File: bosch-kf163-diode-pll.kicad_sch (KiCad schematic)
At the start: 49 parts, among them U1 PLL

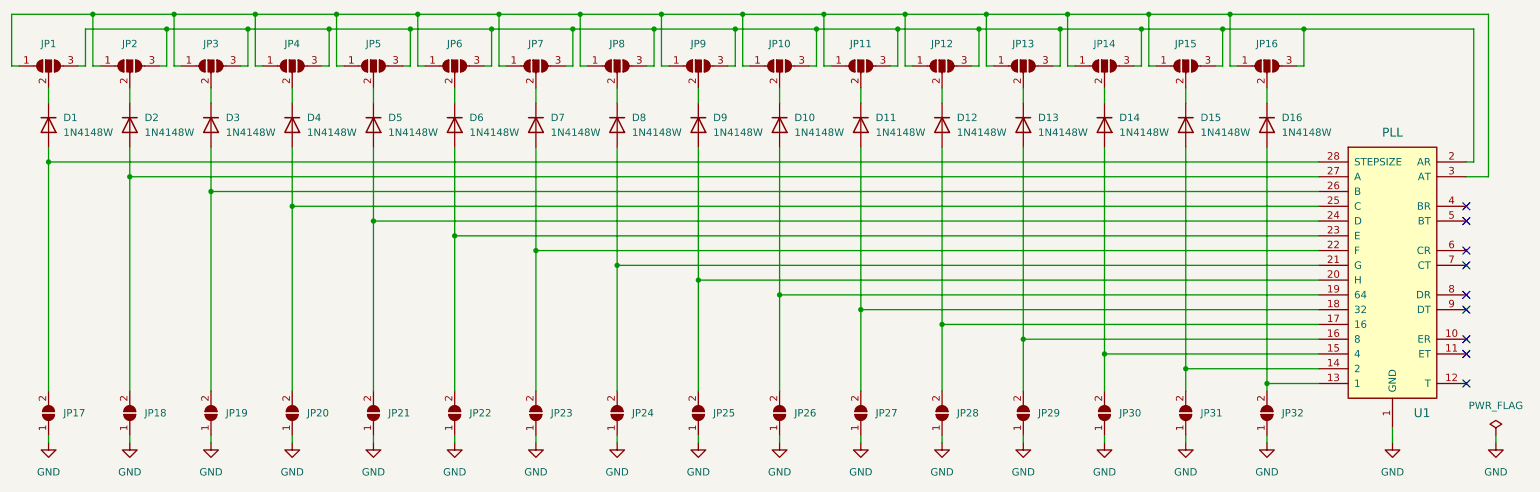
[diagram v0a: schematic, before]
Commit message: changed to smaller diodes, added schematic pdf and gerbers
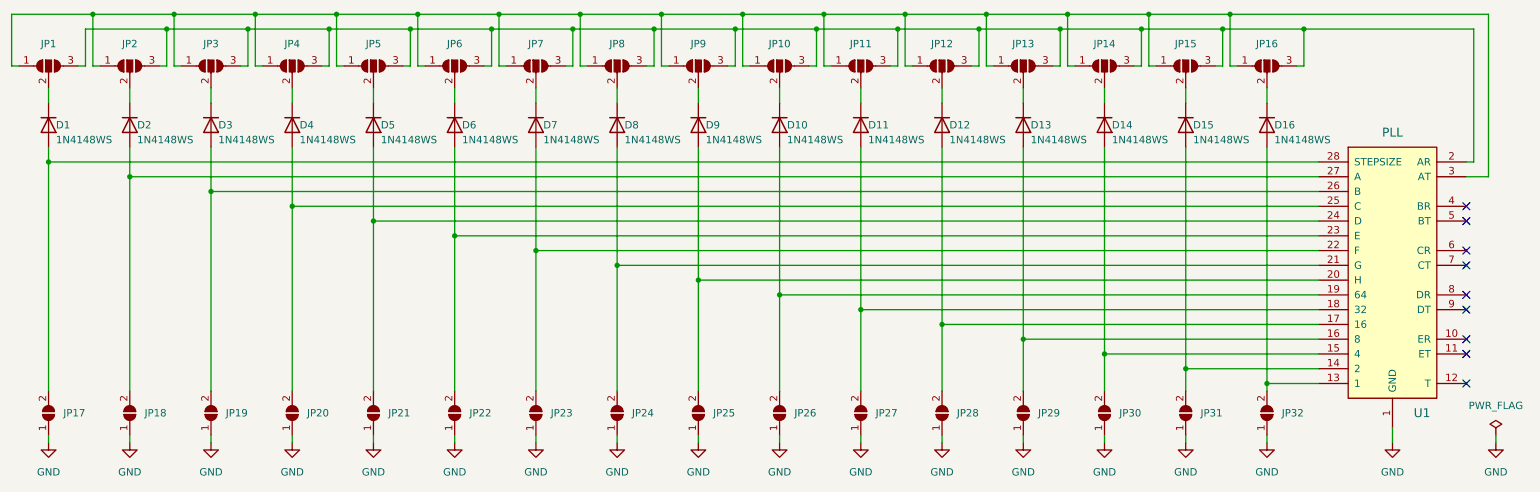
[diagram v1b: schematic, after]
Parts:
- D1, D10, D11, D12, D13, D14, D15, D16, D2, D3, D4, D5, D6, D7, D8, D9: value 1N4148W -> 1N4148WS; footprint Diode_SMD:D_SOD-123 -> Diode_SMD:D_SOD-323; LCSC C84367 -> C108805
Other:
- title: Bosch KFx3/KFx5 Diode PLL -> Bosch KFx3/KFEx5 Diode PLL
